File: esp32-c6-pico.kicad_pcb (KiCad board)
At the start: 4 copper layers, 18 x 39 mm, 65 parts, among them J1 USB4105-GF-A, J2 J2 GPIO / 2.00mm, J3 J3 GPIO / 2.00mm, SW1 RESET, SW2 BOOT, U1 ESP32-C6, U2 AP2112K-3.3, U3 W25Q32JVZPIQ, U4 SN74LV1T125, Y1 40MHz / CL=8pF

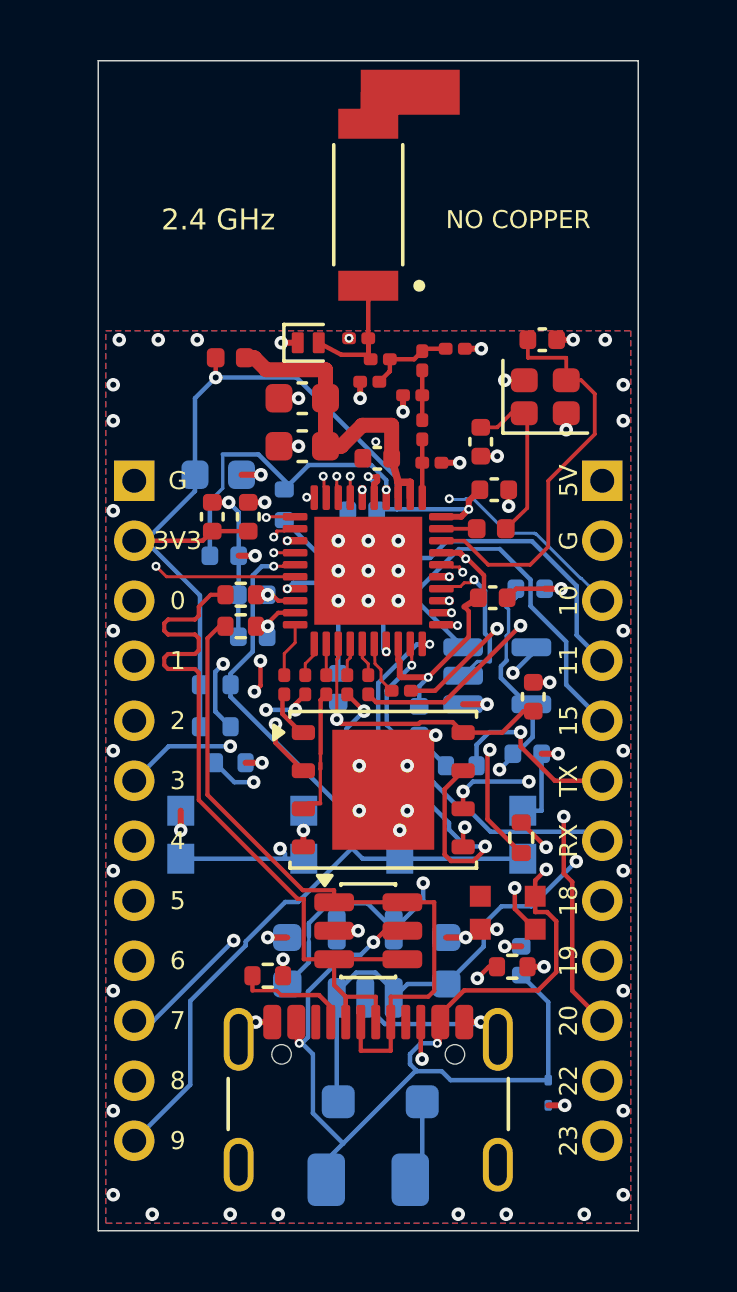
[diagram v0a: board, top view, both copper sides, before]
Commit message: Refine ESP32-C6 Pico layout and project handoff
Update the 20.5 x 32 mm layout, antenna and crystal placement, USB routing, via clearances, and silkscreen logos. Keep RF passives at 0201 and use 0402 for all other resistors and capacitors. Draw ESP32-C6 peripherals directly from U1 pins.

Refresh BOM, placement files, previews, validation reports, and project guidance. Exclude KiCad backup folders, autosaves, and local state on Windows and Linux.

Validation: ERC, DRC, and unconnected counts are zero; all 45 QA checks passed. Verify final file hashes and backup exclusions before commit.
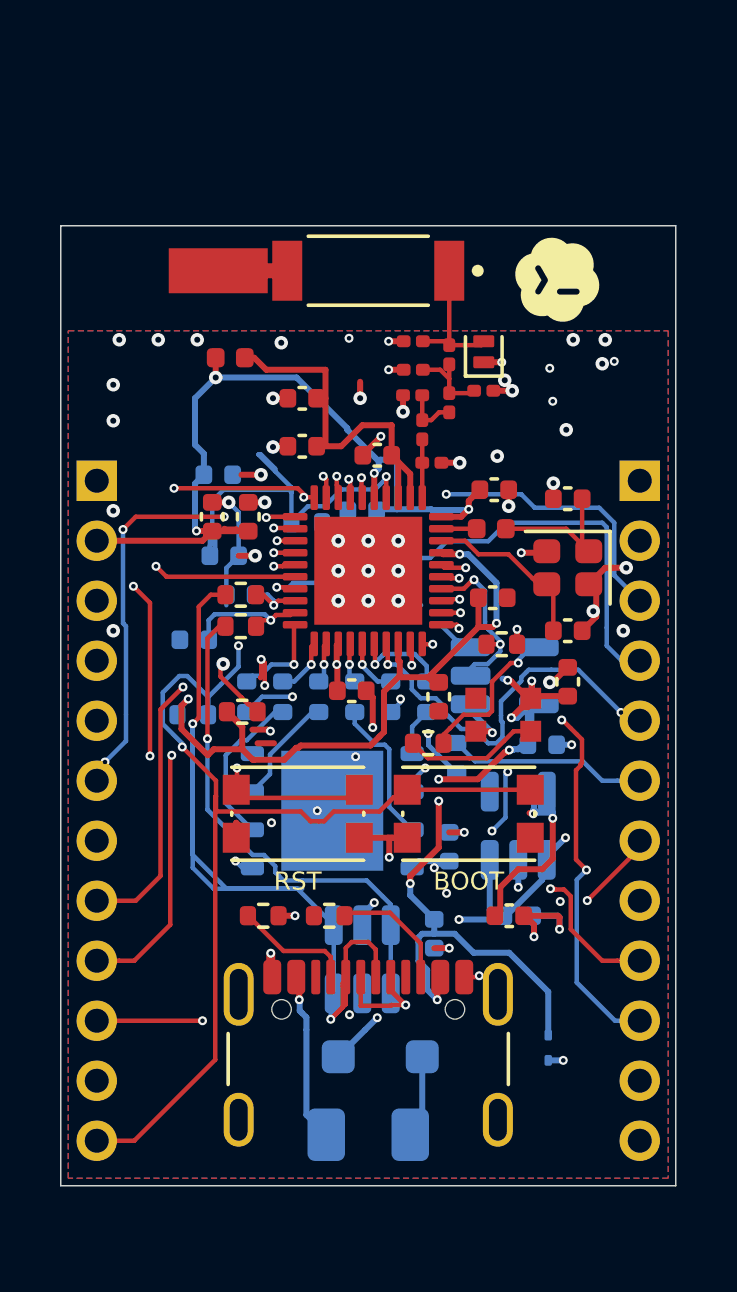
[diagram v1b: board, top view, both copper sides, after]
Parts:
- C13, C26, C7, R16, R9, SW1, SW2: moved to F.Cu
- C19, C20, C22, C8: footprint Capacitor_SMD:C_0603_1608Metric -> Capacitor_SMD:C_0402_1005Metric
- C23: footprint Capacitor_SMD:C_0603_1608Metric -> Capacitor_SMD:C_0402_1005Metric; moved to F.Cu
- C6, D4, J2, J3, U3: moved to B.Cu
- R1, R17, R2, R3, R4, R5: footprint Resistor_SMD:R_0201_0603Metric -> Resistor_SMD:R_0402_1005Metric; moved to B.Cu
- moved R16 9.87 mm to (113.5, 119.5)
- moved C5 9.74 mm to (115.7, 119.0)
- moved C23 7.55 mm to (113.7, 128.5), turned to 0 degrees
- moved U2 6.87 mm to (114.0, 125.5)
- moved D2 6.60 mm to (113.5, 121.8)
- moved R11 6.33 mm to (107.7, 128.5), turned to 180 degrees
- moved D1 5.86 mm to (112.8, 109.7), turned to 90 degrees
- moved Y1 5.75 mm to (115.7, 116.9), turned to 180 degrees
- moved C6 5.73 mm to (111.7, 126.2)
- moved R15 4.42 mm to (111.0, 122.8), turned to 180 degrees
- moved C4 3.47 mm to (115.7, 114.6), turned to 180 degrees
- moved C26 3.34 mm to (115.7, 120.7), turned to 90 degrees
- moved C24 3.04 mm to (111.2, 129.1), turned to -90 degrees
- moved C22 2.83 mm to (114.0, 128.5), turned to 0 degrees
- moved R6 2.30 mm to (111.7, 109.8), turned to 90 degrees
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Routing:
- net GPIO21_LED: track 27.9 -> 6.36 mm
- net SPI_CLK: track 14.6 -> 4.18 mm, vias 3 -> 2
- net SPI_D: track 11.6 -> 1.59 mm, vias 2 -> 0
- net SPI_HD: track 13.6 -> 4.89 mm, vias 2 -> 0
- net +3V3: track 64.0 -> 72.3 mm, vias 6 -> 9
- net XTAL_N: track 13.7 -> 5.75 mm
- net GPIO9_BOOT: track 31.5 -> 38.8 mm, vias 1 -> 3
- net SPI_CS: track 1.63 -> 8.66 mm, vias 0 -> 2
- net USB_D-: track 26.6 -> 33.3 mm, vias 0 -> 2
- net VBUS_USB: track 46.7 -> 40.7 mm, vias 5 -> 10
- net GND: track 47.5 -> 41.5 mm, vias 77 -> 69
- net GPIO4: track 15.4 -> 19.4 mm, vias 1 -> 4
- net CHIP_EN: track 28.6 -> 32.5 mm
- net GPIO11: track 14.2 -> 18.0 mm
- net GPIO7: track 19.0 -> 22.7 mm
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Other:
- board size 18 x 39 mm -> 20.5 x 32 mm
- board text added: "20.5 x 32 mm | 4 layers | 0.8 mm nominal | 0.20 mm drilled vias"
- board text added: "RFANT5220110A0T: axial end copper, 20.5 x 3.5 mm prototype clearance; RF validation required."
- board text removed: "18 x 39 mm | 4 layers | 0.8 mm nominal | 0.20 mm drilled vias"
- board text removed: "2.4 GHz"
- board text removed: "NO COPPER"
- board text removed: "RFANT5220110A0T: 18 x 9 mm clearance. Tune antenna on final assembly."

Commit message: Compact board to 20 x 29 mm and synchronize schematic fields
Move the antenna to the right with a direct feed, place the Codex logo on
the left, and retain 3.8 mm of antenna clearance. Preserve the header
pattern while trimming 0.25 mm from each side of the board.

Fix the 65 schematic field mismatches and refresh placement, BOM,
previews, dimensional checks, and layout documentation.

Validation: ERC, unconnected items, and schematic parity report zero
issues. The two pre-existing C12/C21 hole-clearance violations remain;
independent QA was skipped at the user's request.
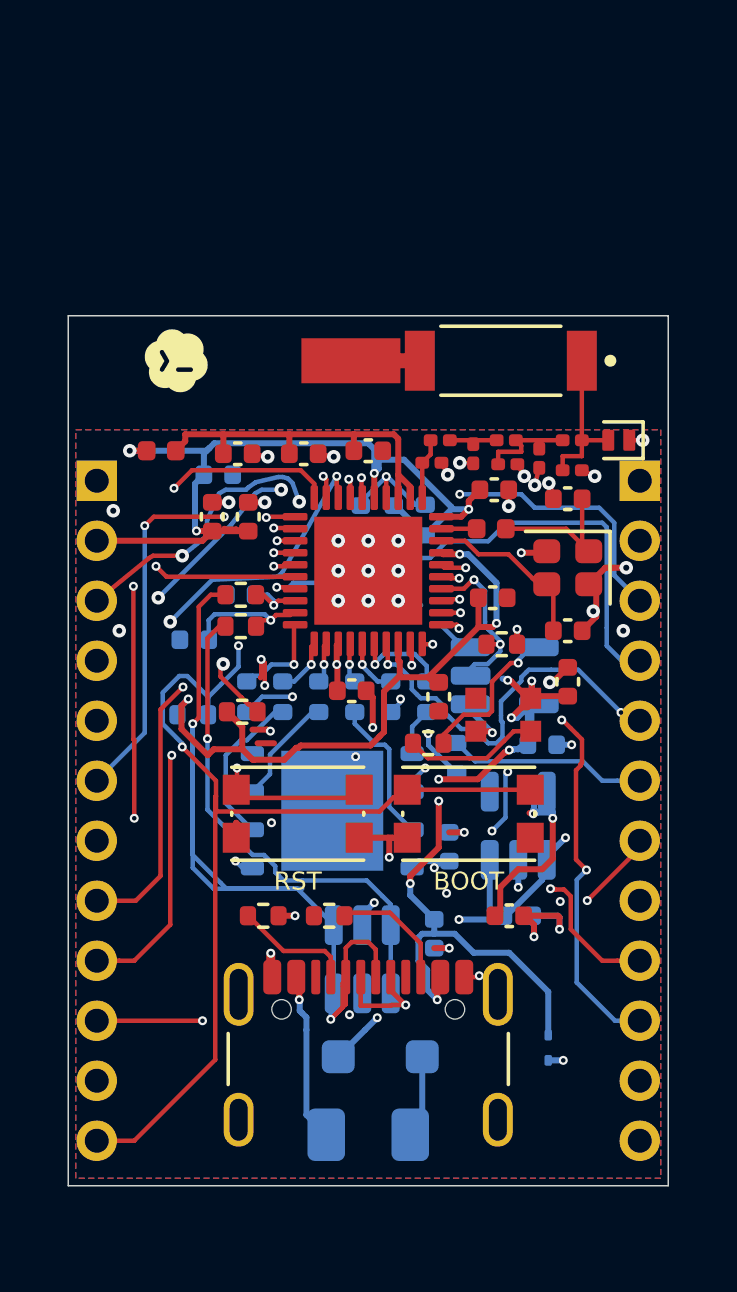
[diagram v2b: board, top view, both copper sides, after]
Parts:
- moved C18 6.82 mm to (115.8, 113.7), turned to 0 degrees
- moved D1 5.38 mm to (117.3, 112.7), turned to 180 degrees
- moved AE1 5.34 mm to (113.4, 110.0)
- moved C17 5.13 mm to (114.7, 113.2), turned to -90 degrees
- moved R6 4.99 mm to (115.8, 112.7), turned to 0 degrees
- moved C21 4.70 mm to (108.8, 115.3), turned to -90 degrees
- moved R7 3.95 mm to (110.9, 115.3), turned to 90 degrees
- moved L2 3.86 mm to (102.1, 113.0)
- moved C19 2.84 mm to (104.7, 113.1), turned to 0 degrees
- moved C2 2.81 mm to (112.5, 113.1), turned to -90 degrees
- moved L3 2.58 mm to (113.7, 113.5)
- moved C16 2.27 mm to (113.6, 112.7), turned to 0 degrees
- moved C12 1.09 mm to (109.8, 115.3), turned to -90 degrees
- moved L1 0.69 mm to (111.4, 112.7), turned to 0 degrees
- moved C11 0.34 mm to (109.0, 113.0), turned to 0 degrees
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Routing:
- net CHIP_EN: track 32.5 -> 21.6 mm
- net GND: track 41.5 -> 32.7 mm, vias 69 -> 48
- net GPIO1: track 14.8 -> 11.6 mm, vias 1 -> 3
- net +3V3: track 72.3 -> 69.4 mm
- net GPIO2: track 15.5 -> 12.9 mm, vias 1 -> 2
- net GPIO10: track 27.5 -> 25.6 mm
- net GPIO0: track 14.1 -> 12.3 mm, vias 1 -> 3
- net V3A: track 11.8 -> 12.6 mm
- net RF_50: track 2.83 -> 3.48 mm
- net ANT_FEED: track 4.64 -> 5.17 mm
- net GPIO4: track 19.4 -> 19.0 mm, vias 4 -> 3
- net GPIO3: track 17.0 -> 16.7 mm, vias 4 -> 3
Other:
- board size 20.5 x 32 mm -> 20 x 29 mm
- board text added: "RFANT5220110A0T: 20 x 29 mm board, antenna on right; 20 x 3.8 mm no-pour region; RF validation required."
- board text removed: "RFANT5220110A0T: axial end copper, 20.5 x 3.5 mm prototype clearance; RF validation required."
